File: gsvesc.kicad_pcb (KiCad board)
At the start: 4 copper layers, 111 x 111 mm, 144 parts, among them J1 Conn_01x06, J10 PHASE_C, J11 PHASE_B, J12 NTC, J13 Conn_01x02, J14 Conn_01x03, J2 Conn_01x06, J3 Conn_01x06, J4 Conn_01x05, J5 Conn_01x03, J6 USB_B_Mini, J7 BAT+, J8 BAT-, J9 PHASE_A, Q1 TPH2R608NH,L1Q, Q2 TPH2R608NH,L1Q, Q3 TPH2R608NH,L1Q, Q4 TPH2R608NH,L1Q, Q5 TPH2R608NH,L1Q, Q6 TPH2R608NH,L1Q, U1 STM32F405RGTx, U10 LM5008MM, U11 SN74LVC1G66DBVR, U12 LM5107, U13 SN74LVC1G66DBVR, U14 TPS5430DDA, U15 LM5107, U16 EYSGJNZWY, U2 SN74LVC1G66DBVR, U3 LM5107, U4 INA240A2, U5 INA240A2, U6 INA240A2, U7 SN74LVC1G66DBVR, U8 SN74LVC1G66DBVR, U9 SN74LVC1G66DBVR, Y1 X50328MSB2GI

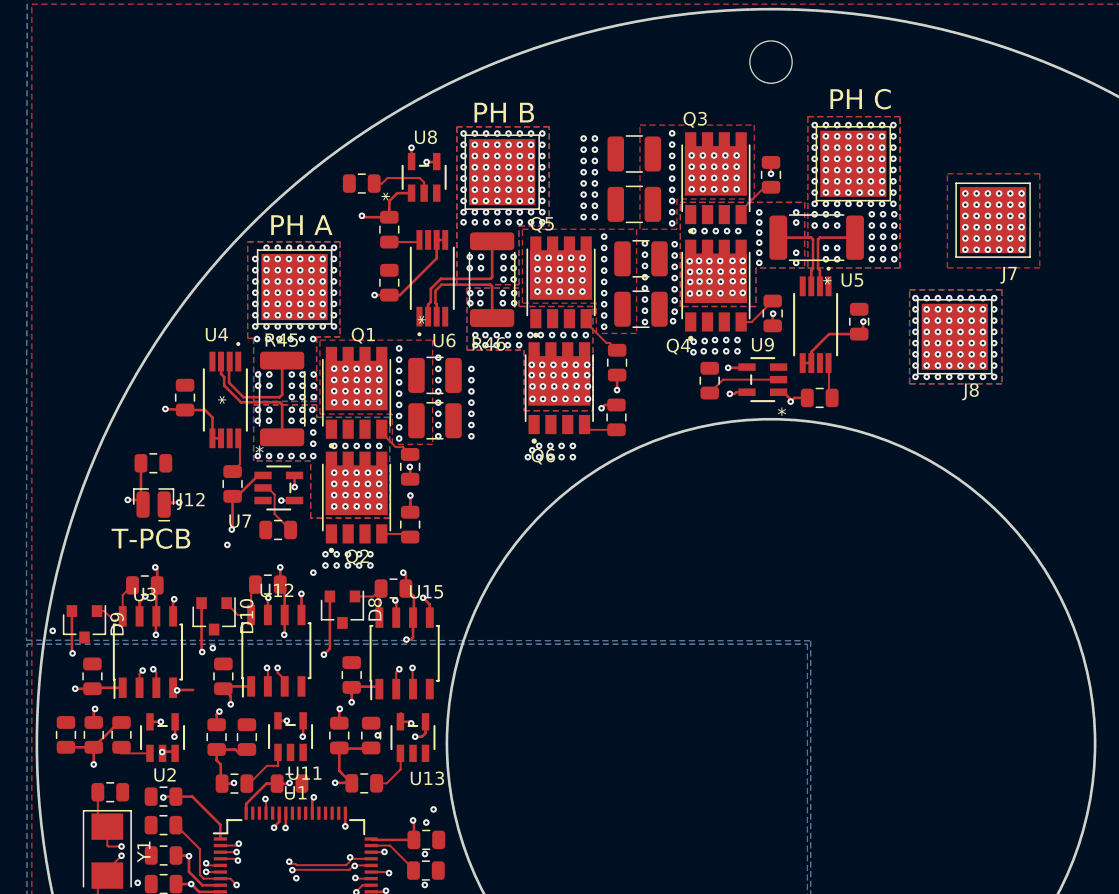
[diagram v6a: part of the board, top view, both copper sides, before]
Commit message: Planes und Vias
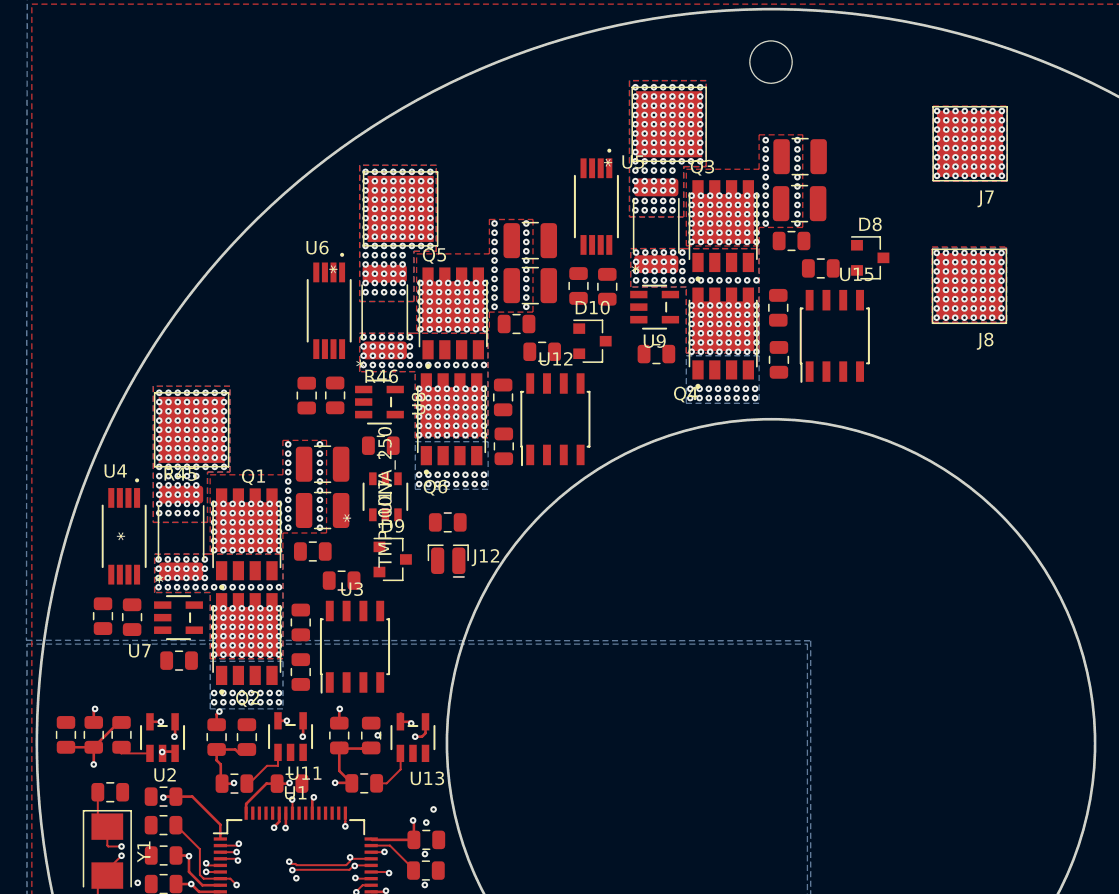
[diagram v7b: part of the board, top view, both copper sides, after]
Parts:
- added U17: TMP100NA_250, gsvesc:TMP100NA_250, F.Cu at (70.8, 81.4)
- R35: value 4k70 -> 7k50
- moved D8 48.0 mm to (107.5, 63.3), turned to 0 degrees
- moved U15 40.4 mm to (104.8, 69.2)
- moved C32 40.4 mm to (103.8, 64.1)
- moved C29 40.1 mm to (100.6, 71.0)
- moved D10 35.4 mm to (86.5, 69.6), turned to 0 degrees
- moved C22 27.4 mm to (79.8, 77.5)
- moved U12 27.4 mm to (83.7, 75.5)
- moved C27 27.2 mm to (82.7, 70.4)
- moved D9 23.8 mm to (71.4, 86.1), turned to 0 degrees
- moved R36 22.7 mm to (75.6, 83.3)
- moved J12 22.7 mm to (75.6, 87.4)
- moved C46 21.4 mm to (85.4, 65.4), turned to 270 degrees
- moved C24 19.9 mm to (70.5, 77.5), turned to 0 degrees
- moved U5 18.8 mm to (86.8, 59.4)
- moved R33 18.1 mm to (87.6, 65.5), turned to 270 degrees
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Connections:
- U1 pad 57: Net-(U1-Pad57) -> /MCU/SERVO
- U1 pad 61: /MCU/SERVO -> /MCU/I2C1_SCL
- U1 pad 62: Net-(U1-Pad62) -> /MCU/I2C1_SDA
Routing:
- net /POWER/CURR_FILTER: track 102.8 -> 1.25 mm, vias 5 -> 1
- net /MCU/CURRENT_3: track 78.6 -> 6.15 mm, vias 3 -> 1
- net /MCU/CURRENT_2: track 68.9 -> 4.06 mm, vias 3 -> 1
- net /Driver/SH_C: track 55.0 -> 1.09 mm, vias 42 -> 81
- net /Driver/GH_C: track 53.7 -> 0.00 mm, vias 2 -> 0
- net /Driver/SH_B: track 47.4 -> 1.08 mm, vias 51 -> 81
- net /Driver/GL_C: track 43.2 -> 0.00 mm, vias 2 -> 0
- net /MCU/ADC_TEMP: track 56.4 -> 17.5 mm, vias 3 -> 2
- net /Driver/SH_A: track 40.0 -> 2.07 mm, vias 46 -> 81
- net /Driver/GH_B: track 35.6 -> 0.00 mm, vias 2 -> 0
- net /Driver/GL_B: track 32.6 -> 0.00 mm, vias 2 -> 0
- net /MCU/CURRENT_1: track 36.5 -> 4.98 mm, vias 2 -> 1
- net /Driver/GH_A: track 29.3 -> 0.00 mm, vias 2 -> 0
- net /Driver/GL_A: track 27.1 -> 0.00 mm, vias 2 -> 0
- net VCC: track 80.1 -> 54.6 mm, vias 36 -> 29
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- removed copper zone on B.Cu, net /Driver/SH_A
- removed copper zone on F.Cu, net /Driver/SH_A
- removed copper zone on In1.Cu, net /Driver/SH_A
- removed copper zone on In2.Cu, net /Driver/SH_A
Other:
- board text removed: "PH A"
- board text removed: "PH B"
- board text removed: "PH C"
- board text removed: "T-PCB"

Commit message: fertig gerouted
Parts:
- added R37: R, Resistor_SMD:R_0805_2012Metric, F.Cu at (79.8, 54.4)
- added R40: R, Resistor_SMD:R_0805_2012Metric, F.Cu at (82.3, 54.4)
- moved U17 25.3 mm to (81.7, 58.5), turned to 180 degrees
- moved C15 8.95 mm to (73.4, 94.5)
- moved C22 8.55 mm to (88.0, 75.1)
- moved C29 8.10 mm to (108.7, 71.2), turned to 270 degrees
- moved R26 3.89 mm to (100.4, 71.0)
- moved R43 3.62 mm to (79.9, 77.5)
- moved R32 3.20 mm to (64.6, 94.1)
- moved R25 3.03 mm to (100.5, 64.9), turned to 270 degrees
- moved R42 2.87 mm to (79.9, 71.0), turned to 270 degrees
- moved R28 2.64 mm to (64.4, 88.0), turned to 270 degrees
- moved C38 1.60 mm to (81.7, 67.0)
- moved C44 1.60 mm to (81.8, 63.6)
- moved C36 1.55 mm to (102.2, 57.2)
- moved C43 1.40 mm to (102.2, 60.6)
- moved D9 0.94 mm to (71.9, 86.9)
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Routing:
- net /MCU/I2C1_SCL: track 0.00 -> 70.7 mm, vias 0 -> 3
- net /POWER/CURR_FILTER: track 1.25 -> 71.5 mm, vias 1 -> 5
- net /MCU/I2C1_SDA: track 0.00 -> 69.5 mm, vias 0 -> 3
- net /MCU/CURRENT_3: track 6.15 -> 75.2 mm, vias 1 -> 3
- net /MCU/L3: track 1.95 -> 66.7 mm, vias 1 -> 2
- net /Driver/SH_C: track 1.09 -> 65.3 mm, vias 81 -> 70
- net /MCU/H3: track 1.99 -> 62.4 mm, vias 1 -> 2
- net /Driver/SH_B: track 1.08 -> 51.4 mm, vias 81 -> 71
- net /MCU/CURRENT_2: track 4.06 -> 52.3 mm, vias 1 -> 3
- net +12V: track 1.62 -> 46.9 mm, vias 8 -> 13
- net /MCU/L2: track 4.98 -> 44.8 mm
- net /MCU/ADC_TEMP: track 17.5 -> 53.0 mm, vias 2 -> 3
- net /MCU/H2: track 5.69 -> 40.8 mm
- net /Driver/SH_A: track 2.07 -> 32.9 mm, vias 81 -> 70
- net VCC: track 54.6 -> 78.9 mm, vias 29 -> 38
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- added copper zone on B.Cu, net /Driver/SH_A
- added copper zone on F.Cu, net /Driver/SH_A
- added copper zone on In1.Cu, net /Driver/SH_A
- added copper zone on In2.Cu, net /Driver/SH_A
